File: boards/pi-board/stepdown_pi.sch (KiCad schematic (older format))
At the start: 0 parts

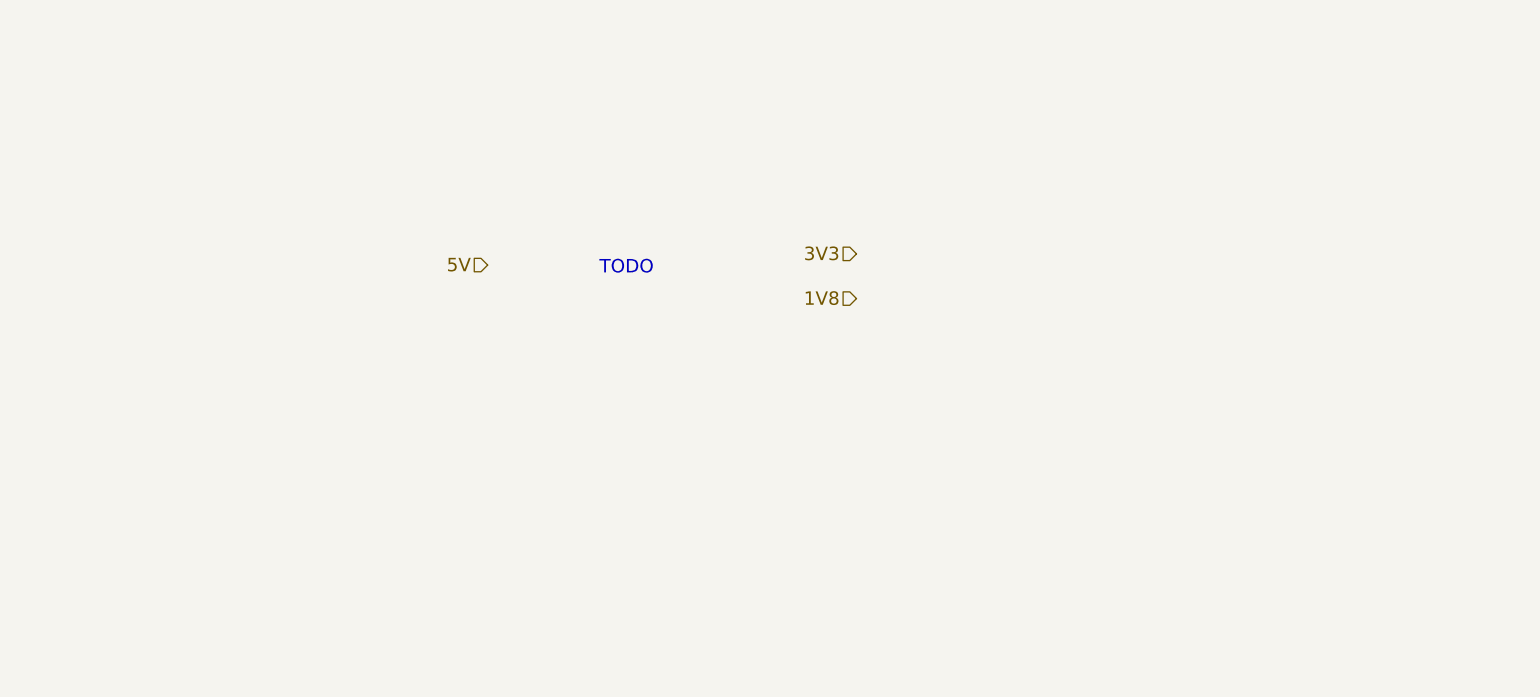
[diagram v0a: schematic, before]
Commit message: boards/pi: added stepdown converter
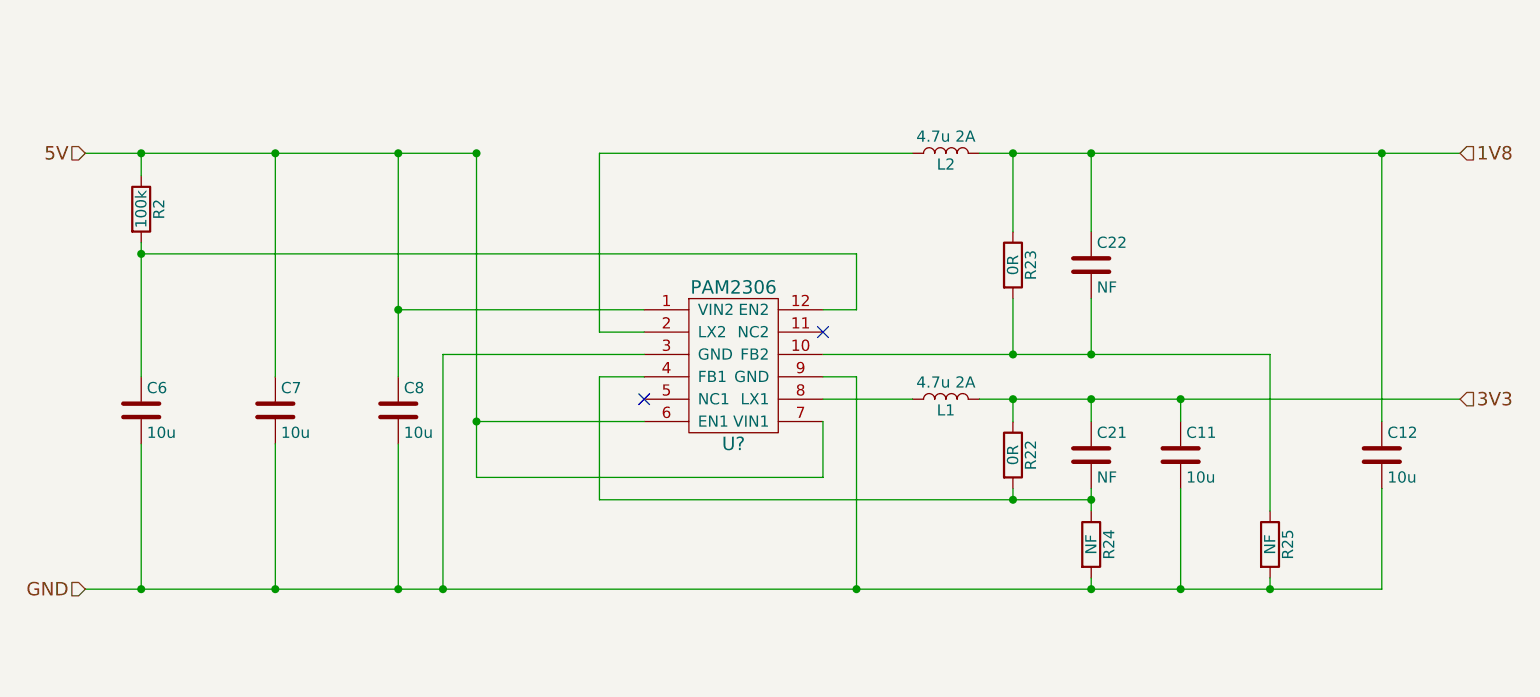
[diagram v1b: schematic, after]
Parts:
- added C11, C12, C6, C7, C8: 10u, symbol C
- added C21, C22: NF, symbol C
- added L1, L2: 4.7u 2A, symbol L
- added R2: 100k, symbol R
- added R22, R23: 0R, symbol R
- added R24, R25: NF, symbol R
- added U?: PAM2306, symbol PAM2306
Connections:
- net 1V8: now also C12.1, C22.1, L2.2, R23.1
- net 3V3: now also C11.1, C21.1, L1.2, R22.1
- net 5V: now also C7.1, C8.1, R2.1, U?.1 (VIN2), U?.6 (EN1), U?.7 (VIN1)
- new net: C22.2, R23.2, R25.1, U?.10 (FB2)
- new net: C6.1, R2.2, U?.12 (EN2)
- new net: L2.1, U?.2 (LX2)
- new net: C21.2, R22.2, R24.1, U?.4 (FB1)
- new net: L1.1, U?.8 (LX1)
- new net GND: C11.2, C12.2, C6.2, C7.2, C8.2, R24.2, R25.2, U?.3 (GND), U?.9 (GND)
- no-connect marks 0 -> 2
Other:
- note removed: "TODO"

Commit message: board/pi: schematics: cleanup, bugfixing, added power LED and testpoints
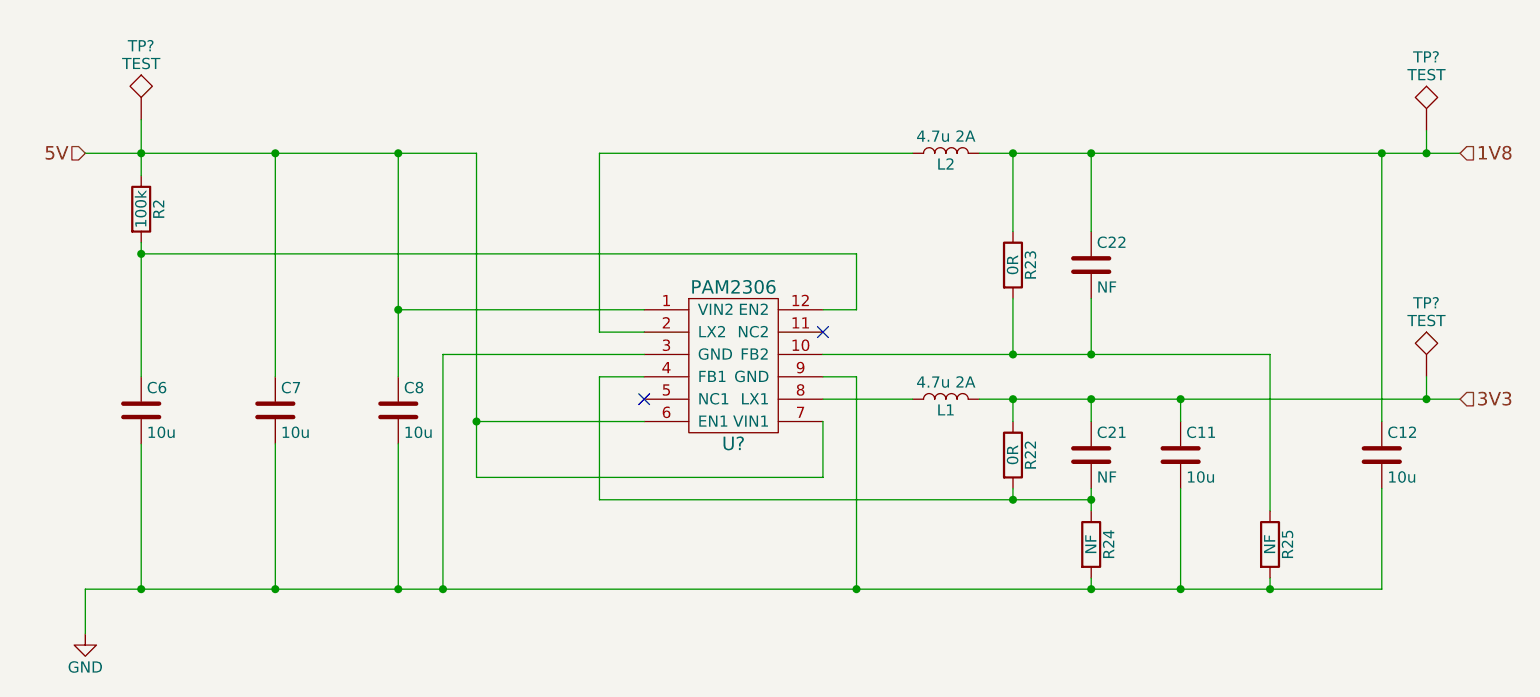
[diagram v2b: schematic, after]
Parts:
- added TP? (x3): TEST, symbol TEST
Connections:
- net 1V8: now also TP?.1
- net 3V3: now also TP?.1
- net 5V: now also TP?.1
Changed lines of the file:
@@
 Comment4 ""
 $EndDescr
-Text HLabel 3150 4500 0    60   Input ~ 0
-GND
 Text HLabel 3150 2550 0    60   Input ~ 0
 5V
@@
 Wire Wire Line
 	4900 3750 5650 3750
-Connection ~ 4900 2550
 Connection ~ 4900 3750
 Wire Wire Line
 	4900 4000 6450 4000
 Wire Wire Line
-	3400 2650 3400 2550
+	3400 2400 3400 2650
 Connection ~ 3400 2550
 Wire Wire Line
@@
 Wire Wire Line
 	3150 4500 8950 4500
+$Comp
+L GND #PWR?
+U 1 1 590BD5E5
+P 3150 4700
+F 0 "#PWR?" H 3150 4450 50  0001 C CNN
+F 1 "GND" H 3150 4550 50  0000 C CNN
+F 2 "" H 3150 4700 50  0001 C CNN
+F 3 "" H 3150 4700 50  0001 C CNN
+	1    3150 4700
+	1    0    0    -1
+$EndComp
+Wire Wire Line
+	3150 4700 3150 4500
+$Comp
+L TEST TP?
+U 1 1 590BEEA7
+P 9150 2450
+F 0 "TP?" H 9150 2750 50  0000 C BNN
+F 1 "TEST" H 9150 2700 50  0000 C CNN
+F 2 "" H 9150 2450 50  0001 C CNN
+F 3 "" H 9150 2450 50  0001 C CNN
+	1    9150 2450
+	1    0    0    -1
+$EndComp
+$Comp
+L TEST TP?
+U 1 1 590BEEFA
+P 9150 3550
+F 0 "TP?" H 9150 3850 50  0000 C BNN
+F 1 "TEST" H 9150 3800 50  0000 C CNN
+F 2 "" H 9150 3550 50  0001 C CNN
+F 3 "" H 9150 3550 50  0001 C CNN
+	1    9150 3550
+	1    0    0    -1
+$EndComp
+Wire Wire Line
+	9150 3550 9150 3650
+Connection ~ 9150 3650
+Wire Wire Line
+	9150 2450 9150 2550
+Connection ~ 9150 2550
+$Comp
+L TEST TP?
+U 1 1 590BF6C0
+P 3400 2400
+F 0 "TP?" H 3400 2700 50  0000 C BNN
+F 1 "TEST" H 3400 2650 50  0000 C CNN
+F 2 "" H 3400 2400 50  0001 C CNN
+F 3 "" H 3400 2400 50  0001 C CNN
+	1    3400 2400
+	1    0    0    -1
+$EndComp
 $EndSCHEMATC

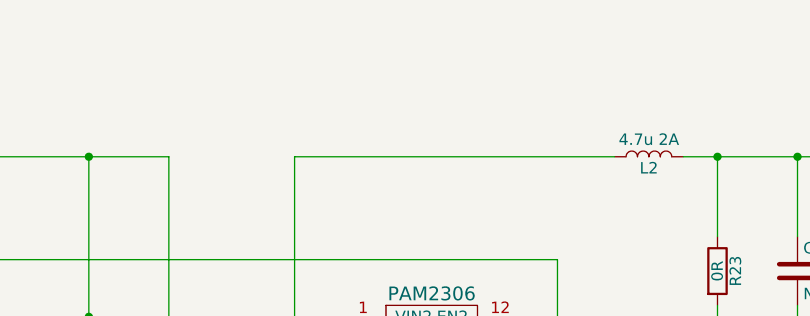
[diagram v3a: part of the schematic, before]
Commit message: schematics/pi: added USB boot wiring
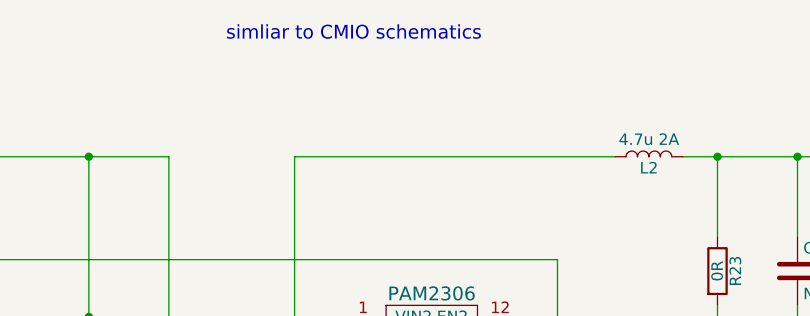
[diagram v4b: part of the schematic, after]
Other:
- note added: "simliar to CMIO schematics"
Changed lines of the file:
@@
 	1    0    0    -1
 $EndComp
+Text Notes 5150 2050 0    60   ~ 0
+simliar to CMIO schematics
 $EndSCHEMATC

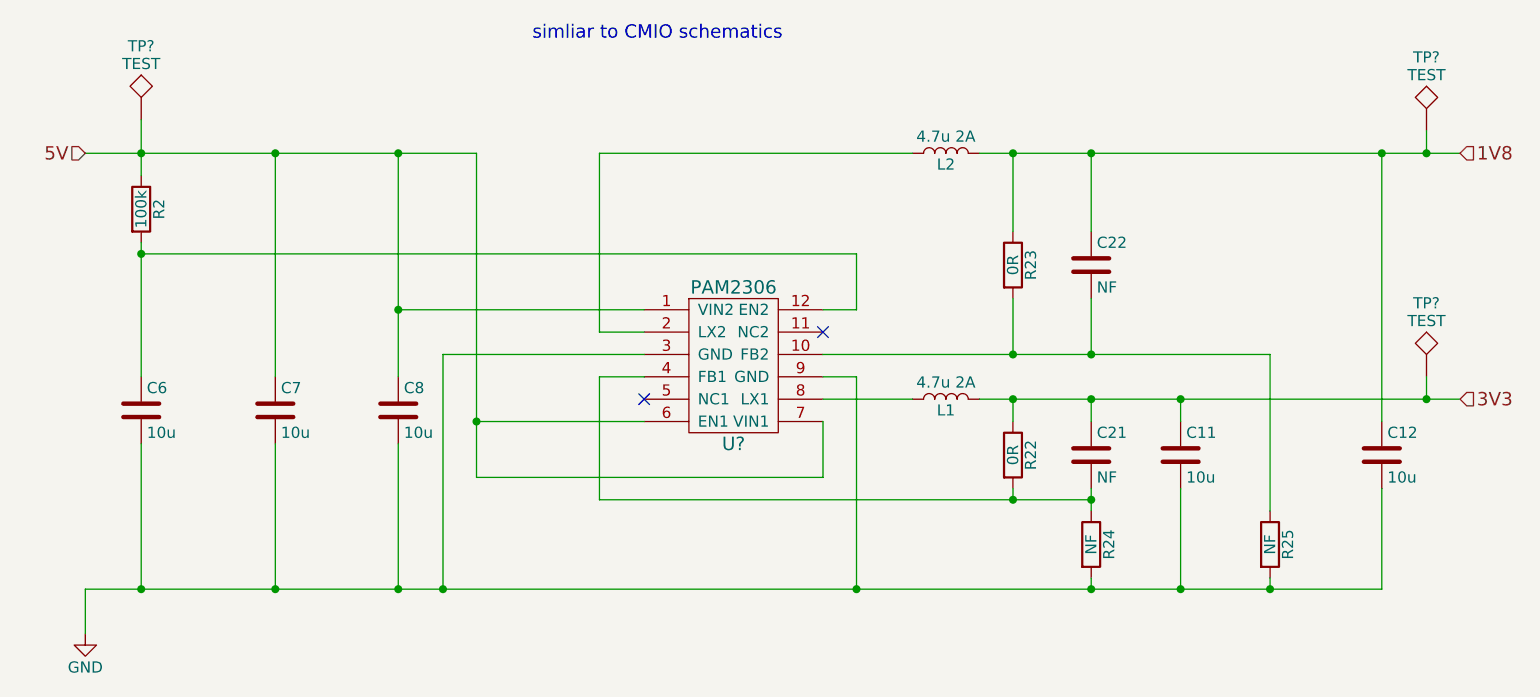
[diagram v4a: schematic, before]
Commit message: schematics/pi: minor corrections, added annotation and most footprints
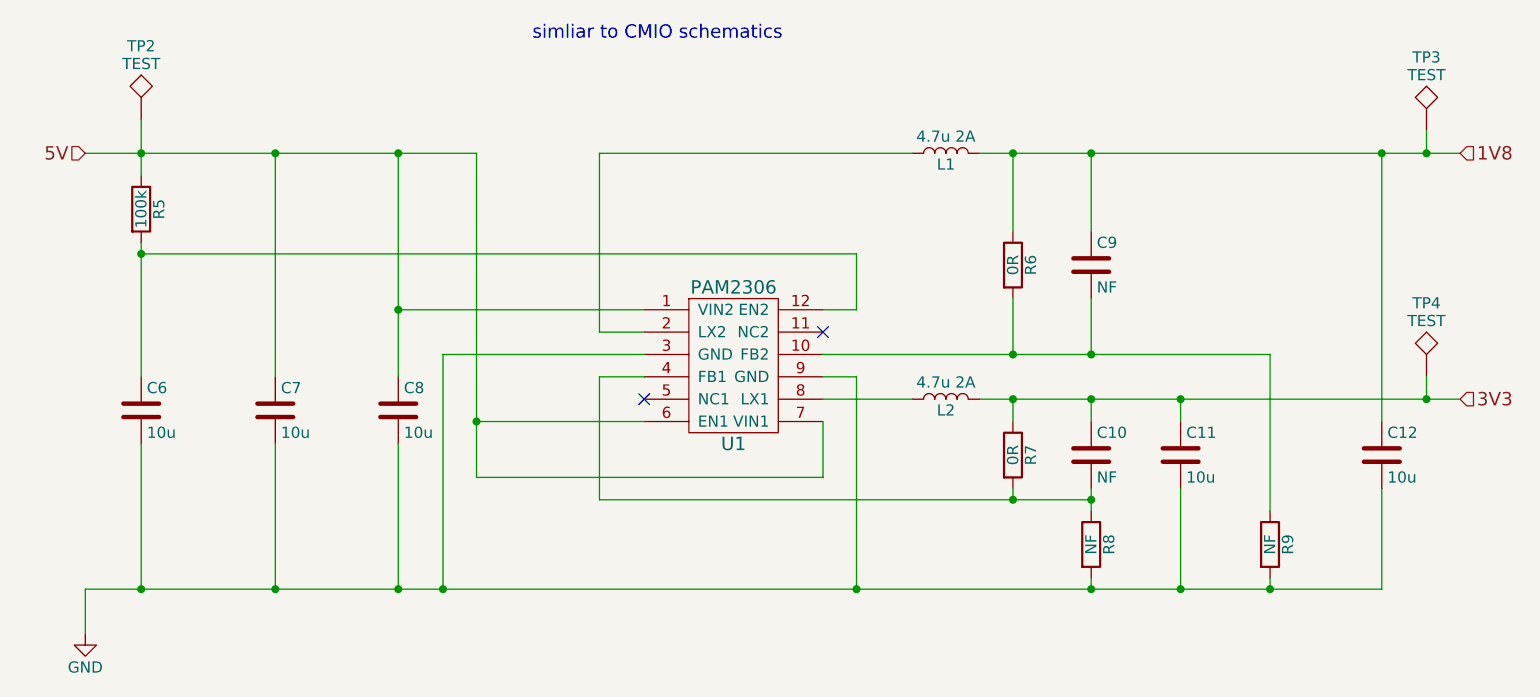
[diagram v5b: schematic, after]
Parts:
- C10: renamed from C21; footprint (none) -> Capacitors_SMD:C_0603_HandSoldering
- C11, C12, C6, C7, C8: footprint (none) -> Capacitors_SMD:C_0603_HandSoldering
- C9: renamed from C22; footprint (none) -> Capacitors_SMD:C_0603_HandSoldering
- L1: renamed from L2; footprint (none) -> Inductors:INDUCTOR_V
- L2: renamed from L1; footprint (none) -> Inductors:INDUCTOR_V
- R5: renamed from R2; footprint (none) -> Resistors_SMD:R_0603
- R6: renamed from R23; footprint (none) -> Resistors_SMD:R_0603
- R7: renamed from R22; footprint (none) -> Resistors_SMD:R_0603
- R8: renamed from R24; footprint (none) -> Resistors_SMD:R_0603
- R9: renamed from R25; footprint (none) -> Resistors_SMD:R_0603
- gave numbers to parts that had none: 4
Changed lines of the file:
@@
 F 0 "C8" H 4575 3800 50  0000 L CNN
 F 1 "10u" H 4575 3600 50  0000 L CNN
-F 2 "" H 4588 3550 50  0001 C CNN
+F 2 "Capacitors_SMD:C_0603_HandSoldering" H 4588 3550 50  0001 C CNN
 F 3 "" H 4550 3700 50  0001 C CNN
 	1    4550 3700
@@
 F 0 "C7" H 4025 3800 50  0000 L CNN
 F 1 "10u" H 4025 3600 50  0000 L CNN
-F 2 "" H 4038 3550 50  0001 C CNN
+F 2 "Capacitors_SMD:C_0603_HandSoldering" H 4038 3550 50  0001 C CNN
 F 3 "" H 4000 3700 50  0001 C CNN
 	1    4000 3700
@@
 F 0 "C6" H 3425 3800 50  0000 L CNN
 F 1 "10u" H 3425 3600 50  0000 L CNN
-F 2 "" H 3438 3550 50  0001 C CNN
+F 2 "Capacitors_SMD:C_0603_HandSoldering" H 3438 3550 50  0001 C CNN
 F 3 "" H 3400 3700 50  0001 C CNN
 	1    3400 3700
@@
 $EndComp
 $Comp
-L PAM2306 U?
+L PAM2306 U1
 U 1 1 59078D7C
 P 6050 3500
-F 0 "U?" H 6050 3150 60  0000 C CNN
+F 0 "U1" H 6050 3150 60  0000 C CNN
 F 1 "PAM2306" H 6050 3850 60  0000 C CNN
 F 2 "" H 6050 3500 60  0001 C CNN
@@
 $EndComp
 $Comp
-L R R2
+L R R5
 U 1 1 59079818
 P 3400 2800
-F 0 "R2" V 3480 2800 50  0000 C CNN
+F 0 "R5" V 3480 2800 50  0000 C CNN
 F 1 "100k" V 3400 2800 50  0000 C CNN
-F 2 "" V 3330 2800 50  0001 C CNN
+F 2 "Resistors_SMD:R_0603" V 3330 2800 50  0001 C CNN
 F 3 "" H 3400 2800 50  0001 C CNN
 	1    3400 2800
@@
 NoConn ~ 6450 3350
 $Comp
-L L L1
+L L L2
 U 1 1 5907A101
 P 7000 3650
-F 0 "L1" V 6950 3650 50  0000 C CNN
+F 0 "L2" V 6950 3650 50  0000 C CNN
 F 1 "4.7u 2A" V 7075 3650 50  0000 C CNN
-F 2 "" H 7000 3650 50  0001 C CNN
+F 2 "Inductors:INDUCTOR_V" H 7000 3650 50  0001 C CNN
 F 3 "" H 7000 3650 50  0001 C CNN
 	1    7000 3650
@@
 $EndComp
 $Comp
-L R R22
+L R R7
 U 1 1 5907A33E
 P 7300 3900
-F 0 "R22" V 7380 3900 50  0000 C CNN
+F 0 "R7" V 7380 3900 50  0000 C CNN
 F 1 "0R" V 7300 3900 50  0000 C CNN
-F 2 "" V 7230 3900 50  0001 C CNN
+F 2 "Resistors_SMD:R_0603" V 7230 3900 50  0001 C CNN
 F 3 "" H 7300 3900 50  0001 C CNN
 	1    7300 3900
@@
 $EndComp
 $Comp
-L C C21
+L C C10
 U 1 1 5907A3A0
 P 7650 3900
-F 0 "C21" H 7675 4000 50  0000 L CNN
+F 0 "C10" H 7675 4000 50  0000 L CNN
 F 1 "NF" H 7675 3800 50  0000 L CNN
-F 2 "" H 7688 3750 50  0001 C CNN
+F 2 "Capacitors_SMD:C_0603_HandSoldering" H 7688 3750 50  0001 C CNN
 F 3 "" H 7650 3900 50  0001 C CNN
 	1    7650 3900
@@
 $EndComp
 $Comp
-L R R24
+L R R8
 U 1 1 5907A5C3
 P 7650 4300
-F 0 "R24" V 7730 4300 50  0000 C CNN
+F 0 "R8" V 7730 4300 50  0000 C CNN
 F 1 "NF" V 7650 4300 50  0000 C CNN
-F 2 "" V 7580 4300 50  0001 C CNN
+F 2 "Resistors_SMD:R_0603" V 7580 4300 50  0001 C CNN
 F 3 "" H 7650 4300 50  0001 C CNN
 	1    7650 4300
@@
 F 0 "C11" H 8075 4000 50  0000 L CNN
 F 1 "10u" H 8075 3800 50  0000 L CNN
-F 2 "" H 8088 3750 50  0001 C CNN
+F 2 "Capacitors_SMD:C_0603_HandSoldering" H 8088 3750 50  0001 C CNN
 F 3 "" H 8050 3900 50  0001 C CNN
 	1    8050 3900
@@
 $EndComp
 $Comp
-L L L2
+L L L1
 U 1 1 5907AE5A
 P 7000 2550
-F 0 "L2" V 6950 2550 50  0000 C CNN
+F 0 "L1" V 6950 2550 50  0000 C CNN
 F 1 "4.7u 2A" V 7075 2550 50  0000 C CNN
-F 2 "" H 7000 2550 50  0001 C CNN
+F 2 "Inductors:INDUCTOR_V" H 7000 2550 50  0001 C CNN
 F 3 "" H 7000 2550 50  0001 C CNN
 	1    7000 2550
@@
 $EndComp
 $Comp
-L R R23
+L R R6
 U 1 1 5907B186
 P 7300 3050
-F 0 "R23" V 7380 3050 50  0000 C CNN
+F 0 "R6" V 7380 3050 50  0000 C CNN
 F 1 "0R" V 7300 3050 50  0000 C CNN
-F 2 "" V 7230 3050 50  0001 C CNN
+F 2 "Resistors_SMD:R_0603" V 7230 3050 50  0001 C CNN
 F 3 "" H 7300 3050 50  0001 C CNN
 	1    7300 3050
@@
 3V3
 $Comp
-L C C22
+L C C9
 U 1 1 5907B3B6
 P 7650 3050
-F 0 "C22" H 7675 3150 50  0000 L CNN
+F 0 "C9" H 7675 3150 50  0000 L CNN
 F 1 "NF" H 7675 2950 50  0000 L CNN
-F 2 "" H 7688 2900 50  0001 C CNN
+F 2 "Capacitors_SMD:C_0603_HandSoldering" H 7688 2900 50  0001 C CNN
 F 3 "" H 7650 3050 50  0001 C CNN
 	1    7650 3050
@@
 $EndComp
 $Comp
-L R R25
+L R R9
 U 1 1 5907B5B0
 P 8450 4300
-F 0 "R25" V 8530 4300 50  0000 C CNN
+F 0 "R9" V 8530 4300 50  0000 C CNN
 F 1 "NF" V 8450 4300 50  0000 C CNN
-F 2 "" V 8380 4300 50  0001 C CNN
+F 2 "Resistors_SMD:R_0603" V 8380 4300 50  0001 C CNN
 F 3 "" H 8450 4300 50  0001 C CNN
 	1    8450 4300
@@
 F 0 "C12" H 8975 4000 50  0000 L CNN
 F 1 "10u" H 8975 3800 50  0000 L CNN
-F 2 "" H 8988 3750 50  0001 C CNN
+F 2 "Capacitors_SMD:C_0603_HandSoldering" H 8988 3750 50  0001 C CNN
 F 3 "" H 8950 3900 50  0001 C CNN
 	1    8950 3900
@@
 	3150 4500 8950 4500
 $Comp
-L GND #PWR011
+L GND #PWR016
 U 1 1 590BD5E5
 P 3150 4700
-F 0 "#PWR011" H 3150 4450 50  0001 C CNN
+F 0 "#PWR016" H 3150 4450 50  0001 C CNN
 F 1 "GND" H 3150 4550 50  0000 C CNN
 F 2 "" H 3150 4700 50  0001 C CNN
@@
 	3150 4700 3150 4500
 $Comp
-L TEST TP?
+L TEST TP3
 U 1 1 590BEEA7
 P 9150 2450
-F 0 "TP?" H 9150 2750 50  0000 C BNN
+F 0 "TP3" H 9150 2750 50  0000 C BNN
 F 1 "TEST" H 9150 2700 50  0000 C CNN
 F 2 "" H 9150 2450 50  0001 C CNN
@@
 $EndComp
 $Comp
-L TEST TP?
+L TEST TP4
 U 1 1 590BEEFA
 P 9150 3550
-F 0 "TP?" H 9150 3850 50  0000 C BNN
+F 0 "TP4" H 9150 3850 50  0000 C BNN
 F 1 "TEST" H 9150 3800 50  0000 C CNN
 F 2 "" H 9150 3550 50  0001 C CNN
@@
 Connection ~ 9150 2550
 $Comp
-L TEST TP?
+L TEST TP2
 U 1 1 590BF6C0
 P 3400 2400
-F 0 "TP?" H 3400 2700 50  0000 C BNN
+F 0 "TP2" H 3400 2700 50  0000 C BNN
 F 1 "TEST" H 3400 2650 50  0000 C CNN
 F 2 "" H 3400 2400 50  0001 C CNN

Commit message: schematics/pi: added missing footprints
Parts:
- U1: footprint (none) -> rx-viper:pam2306
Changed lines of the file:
@@
 F 0 "U1" H 6050 3150 60  0000 C CNN
 F 1 "PAM2306" H 6050 3850 60  0000 C CNN
-F 2 "" H 6050 3500 60  0001 C CNN
+F 2 "rx-viper:pam2306" H 6050 3500 60  0001 C CNN
 F 3 "" H 6050 3500 60  0001 C CNN
 	1    6050 3500

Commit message: schematics/pi: choose correct footprints for L and NMOS
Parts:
- L1, L2: footprint Inductors:INDUCTOR_V -> Inductors:Inductor_Taiyo-Yuden_NR-50xx_HandSoldering
- TP2, TP3, TP4: footprint (none) -> Measurement_Points:Measurement_Point_Round-SMD-Pad_Small
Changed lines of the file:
@@
 F 0 "L2" V 6950 3650 50  0000 C CNN
 F 1 "4.7u 2A" V 7075 3650 50  0000 C CNN
-F 2 "Inductors:INDUCTOR_V" H 7000 3650 50  0001 C CNN
+F 2 "Inductors:Inductor_Taiyo-Yuden_NR-50xx_HandSoldering" H 7000 3650 50  0001 C CNN
 F 3 "" H 7000 3650 50  0001 C CNN
 	1    7000 3650
@@
 F 0 "L1" V 6950 2550 50  0000 C CNN
 F 1 "4.7u 2A" V 7075 2550 50  0000 C CNN
-F 2 "Inductors:INDUCTOR_V" H 7000 2550 50  0001 C CNN
+F 2 "Inductors:Inductor_Taiyo-Yuden_NR-50xx_HandSoldering" H 7000 2550 50  0001 C CNN
 F 3 "" H 7000 2550 50  0001 C CNN
 	1    7000 2550
@@
 F 0 "TP3" H 9150 2750 50  0000 C BNN
 F 1 "TEST" H 9150 2700 50  0000 C CNN
-F 2 "" H 9150 2450 50  0001 C CNN
+F 2 "Measurement_Points:Measurement_Point_Round-SMD-Pad_Small" H 9150 2450 50  0001 C CNN
 F 3 "" H 9150 2450 50  0001 C CNN
 	1    9150 2450
@@
 F 0 "TP4" H 9150 3850 50  0000 C BNN
 F 1 "TEST" H 9150 3800 50  0000 C CNN
-F 2 "" H 9150 3550 50  0001 C CNN
+F 2 "Measurement_Points:Measurement_Point_Round-SMD-Pad_Small" H 9150 3550 50  0001 C CNN
 F 3 "" H 9150 3550 50  0001 C CNN
 	1    9150 3550
@@
 F 0 "TP2" H 3400 2700 50  0000 C BNN
 F 1 "TEST" H 3400 2650 50  0000 C CNN
-F 2 "" H 3400 2400 50  0001 C CNN
+F 2 "Measurement_Points:Measurement_Point_Round-SMD-Pad_Small" H 3400 2400 50  0001 C CNN
 F 3 "" H 3400 2400 50  0001 C CNN
 	1    3400 2400
